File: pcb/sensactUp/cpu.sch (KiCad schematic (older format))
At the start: 25 parts, among them P16 CONN_01X04, P17 CONN_01X04, P3 CONN_01X02, SW1 SW_PUSH, SW2 SW_PUSH, SW3 SW_PUSH, X1 8MHz

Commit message: Huge Refactoring; still untested
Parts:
- removed C10, C11, C4, C7, C8, C9: 100n, Capacitors_SMD:C_0805_HandSoldering, symbol C-RESCUE-multiupbox
- removed C5, C6: 27p, Capacitors_SMD:C_0805_HandSoldering, symbol C-RESCUE-multiupbox
- removed D19: LED, Resistors_SMD:R_0805_HandSoldering, symbol LED-RESCUE-multiupbox
- removed L1: INDUCTOR, Inductors_NEOSID:Neosid_Inductor_SM1206, symbol INDUCTOR
- removed P16, P17: CONN_01X04, Pin_Headers:Pin_Header_Straight_1x04, symbol CONN_01X04
- removed P3: CONN_01X02, Pin_Headers:Pin_Header_Straight_1x02, symbol CONN_01X02
- removed R24, R25, R3, R31, R32: 10k, Resistors_SMD:R_0805_HandSoldering, symbol R-RESCUE-multiupbox
- removed R30: 330R, Resistors_SMD:R_0805_HandSoldering, symbol R-RESCUE-multiupbox
- removed R5: 1M, Resistors_SMD:R_0805_HandSoldering, symbol R-RESCUE-multiupbox
- removed SW1, SW2, SW3: SW_PUSH, Discret:SW_PUSH_SMALL, symbol SW_PUSH
- removed U?: STM32F103CB, LQFP48, symbol STM32F103CB
- removed X1: 8MHz, Crystals:Crystal_HC49-U_Vertical, symbol CRYSTAL
- added C15: 4u7, Capacitors_SMD:C_1206_HandSoldering, symbol C
- added C16, C17, C18: u1, Capacitors_SMD:C_0805_HandSoldering, symbol C
- added C19: 10n, Capacitors_SMD:C_0805_HandSoldering, symbol C
- added C20: 1u, Capacitors_SMD:C_0805_HandSoldering, symbol C
- added C7, C8: 22p, Capacitors_SMD:C_0805_HandSoldering, symbol C
- added FB1: FILTER, Resistors_SMD:R_1206_HandSoldering, symbol FILTER
- added P7: CONN_01X06, sensact:MicroUsbVertical, symbol CONN_01X06
- added R10: M1, Resistors_SMD:R_0805_HandSoldering, symbol R
- added R7: 220R, Resistors_SMD:R_0805_HandSoldering, symbol R
- added U3: STM32F072C8Tx, sensact:LQFP-48_7x7mm_Pitch0.5mm_handsolder, symbol STM32F072C8Tx
- added Y1: Crystal_GND24, sensact:quartz3225, symbol Crystal_GND24
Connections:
- net labels added: +3.3VA, CANR, CANT, INT1, INT2, INT3, IO1, IO2, IO3, IO4, IO5, IO6, IO7, IO8, ROTA, ROTB, ROTD, RX, SCL, SCL1, SDA, SDA1, SHDN, SWCLK, SWDIO, TX, USBM, USBP, WS2812, xROTA, xROTB, xROTD
- net labels removed: BOOT0, PA0, PA1, PA10, PA11, PA12, PA13, PA14, PA15, PA2, PA3, PA4, PA5, PA6, PA7, PA8, PA9, PA[0..15], PB0, PB1, PB10, PB11, PB12, PB13, PB14, PB15, PB2, PB3, PB4, PB5, PB6, PB7, PB8, PB9, PB[0..15], PC0, PC1, PC10, PC11, PC12, PC13, PC14, PC15, PC2, PC3, PC4, PC5, PC6, PC7, PC8, PC9, PC[0..15], PD2
- wire segments 118 -> 67
- no-connect marks 1 -> 5
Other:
- note removed: "DCF77-Modul (Pollin)"
- note removed: "Programmer-Anschluss"
- note removed: "i2c-Anschluss"

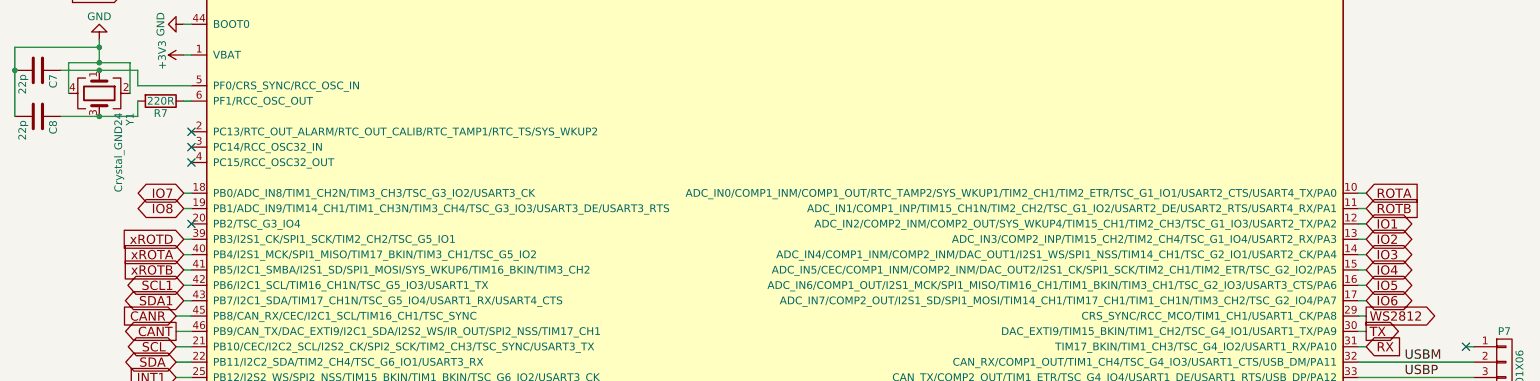
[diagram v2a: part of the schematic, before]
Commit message: SensactUP gets LIN-Port and alternative 5V Power Supply
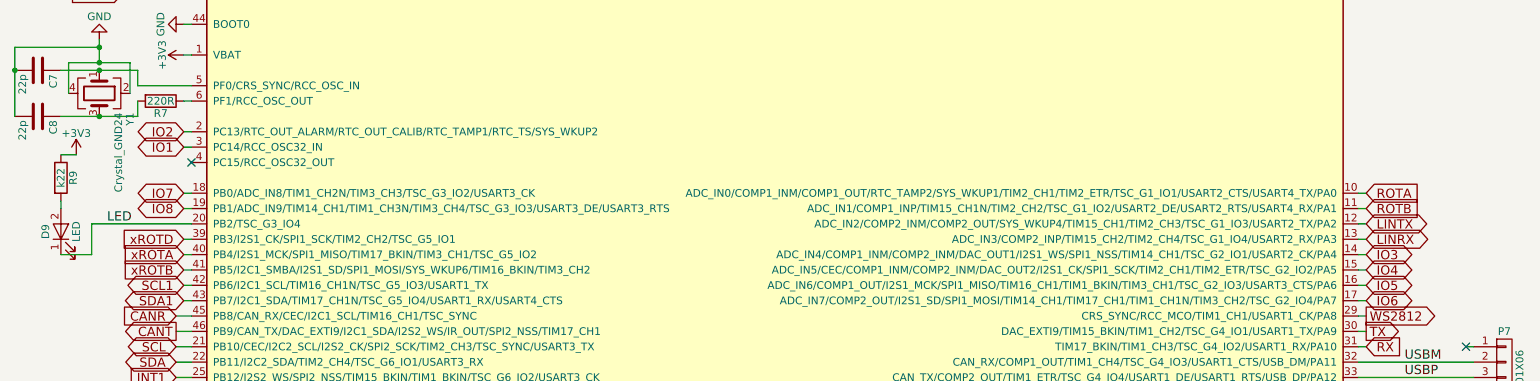
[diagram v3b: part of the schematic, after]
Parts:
- added D9: LED, sensact:LED_0805_handsolder, symbol LED
- added R9: k22, Resistors_SMD:R_0805_HandSoldering, symbol R
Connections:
- net +3V3: now also R9.1
- net IO1: now also U3.3 (PC14/RCC_OSC32_IN); no longer U3.12 (ADC_IN2/COMP2_INM/COMP2_OUT/SYS_WKUP4/TIM15_CH1/TIM2_CH3/TSC_G1_IO3/USART2_TX/PA2)
- net IO2: now also U3.2 (PC13/RTC_OUT_ALARM/RTC_OUT_CALIB/RTC_TAMP1/RTC_TS/SYS_WKUP2); no longer U3.13 (ADC_IN3/COMP2_INP/TIM15_CH2/TIM2_CH4/TSC_G1_IO4/USART2_RX/PA3)
- net LED: now reaches U3.20 (PB2/TSC_G3_IO4)
- net LED: now also D9.1 (K)
- new net: D9.2 (A), R9.2
- new net LINRX: U3.13 (ADC_IN3/COMP2_INP/TIM15_CH2/TIM2_CH4/TSC_G1_IO4/USART2_RX/PA3)
- new net LINTX: U3.12 (ADC_IN2/COMP2_INM/COMP2_OUT/SYS_WKUP4/TIM15_CH1/TIM2_CH3/TSC_G1_IO3/USART2_TX/PA2)
- no-connect marks 5 -> 2
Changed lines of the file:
@@
 LIBS:relays
 LIBS:sensact
+LIBS:mechanical
 LIBS:sensactUp-cache
 EELAYER 25 0
@@
 $EndComp
 $Comp
-L +3V3 #PWR031
+L +3V3 #PWR035
 U 1 1 58B75879
 P 5350 1650
-F 0 "#PWR031" H 5350 1500 50  0001 C CNN
+F 0 "#PWR035" H 5350 1500 50  0001 C CNN
 F 1 "+3V3" H 5350 1790 50  0000 C CNN
 F 2 "" H 5350 1650 50  0000 C CNN
@@
 $EndComp
 $Comp
-L +3V3 #PWR032
+L +3V3 #PWR036
 U 1 1 58B7589B
 P 5600 1650
-F 0 "#PWR032" H 5600 1500 50  0001 C CNN
+F 0 "#PWR036" H 5600 1500 50  0001 C CNN
 F 1 "+3V3" H 5600 1790 50  0000 C CNN
 F 2 "" H 5600 1650 50  0000 C CNN
@@
 Connection ~ 5350 1650
 $Comp
-L +3.3VA #PWR033
+L +3.3VA #PWR037
 U 1 1 58B75979
 P 5500 1450
-F 0 "#PWR033" H 5500 1300 50  0001 C CNN
+F 0 "#PWR037" H 5500 1300 50  0001 C CNN
 F 1 "+3.3VA" H 5500 1590 50  0000 C CNN
 F 2 "" H 5500 1450 50  0000 C CNN
@@
 Connection ~ 4700 1150
 $Comp
-L +3.3VA #PWR034
+L +3.3VA #PWR038
 U 1 1 58B759CE
 P 4800 950
-F 0 "#PWR034" H 4800 800 50  0001 C CNN
+F 0 "#PWR038" H 4800 800 50  0001 C CNN
 F 1 "+3.3VA" H 4800 1090 50  0000 C CNN
 F 2 "" H 4800 950 50  0000 C CNN
@@
 Connection ~ 3450 1150
 $Comp
-L +3V3 #PWR035
+L +3V3 #PWR039
 U 1 1 58B75AF2
 P 3550 1100
-F 0 "#PWR035" H 3550 950 50  0001 C CNN
+F 0 "#PWR039" H 3550 950 50  0001 C CNN
 F 1 "+3V3" H 3550 1240 50  0000 C CNN
 F 2 "" H 3550 1100 50  0000 C CNN
@@
 Connection ~ 3450 1450
 $Comp
-L GND #PWR036
+L GND #PWR040
 U 1 1 58B75BBF
 P 3550 1500
-F 0 "#PWR036" H 3550 1250 50  0001 C CNN
+F 0 "#PWR040" H 3550 1250 50  0001 C CNN
 F 1 "GND" H 3550 1350 50  0000 C CNN
 F 2 "" H 3550 1500 50  0000 C CNN
@@
 Connection ~ 3550 1450
 $Comp
-L GND #PWR037
+L GND #PWR041
 U 1 1 58B75C63
 P 5450 5450
-F 0 "#PWR037" H 5450 5200 50  0001 C CNN
+F 0 "#PWR041" H 5450 5200 50  0001 C CNN
 F 1 "GND" H 5450 5300 50  0000 C CNN
 F 2 "" H 5450 5450 50  0000 C CNN
@@
 	1700 2200 1250 2200
 $Comp
-L GND #PWR038
+L GND #PWR042
 U 1 1 58B775D8
 P 1650 2400
-F 0 "#PWR038" H 1650 2150 50  0001 C CNN
+F 0 "#PWR042" H 1650 2150 50  0001 C CNN
 F 1 "GND" H 1650 2250 50  0000 C CNN
 F 2 "" H 1650 2400 50  0000 C CNN
@@
 $EndComp
 $Comp
-L +3V3 #PWR039
+L +3V3 #PWR043
 U 1 1 58B775FC
 P 1650 2600
-F 0 "#PWR039" H 1650 2450 50  0001 C CNN
+F 0 "#PWR043" H 1650 2450 50  0001 C CNN
 F 1 "+3V3" H 1650 2740 50  0000 C CNN
 F 2 "" H 1650 2600 50  0000 C CNN
@@
 	900  2650 900  2850
 $Comp
-L GND #PWR040
+L GND #PWR044
 U 1 1 58B7775E
 P 1100 2500
-F 0 "#PWR040" H 1100 2250 50  0001 C CNN
+F 0 "#PWR044" H 1100 2250 50  0001 C CNN
 F 1 "GND" H 1100 2350 50  0000 C CNN
 F 2 "" H 1100 2500 50  0000 C CNN
@@
 ROTB
 Text GLabel 9350 3700 2    60   BiDi ~ 0
-IO1
+LINTX
 Text GLabel 9350 3800 2    60   BiDi ~ 0
-IO2
+LINRX
 Text GLabel 9350 3900 2    60   BiDi ~ 0
 IO3
@@
 	9850 4800 10050 4800
 $Comp
-L GND #PWR041
+L GND #PWR045
 U 1 1 58B845F6
 P 10050 5150
-F 0 "#PWR041" H 10050 4900 50  0001 C CNN
+F 0 "#PWR045" H 10050 4900 50  0001 C CNN
 F 1 "GND" H 10050 5000 50  0000 C CNN
 F 2 "" H 10050 5150 50  0000 C CNN
@@
 Wire Wire Line
 	1700 4000 1650 4000
-NoConn ~ 1700 3100
-NoConn ~ 1700 3200
 NoConn ~ 1700 3300
-NoConn ~ 1700 3700
 Text Label 9600 4600 0    60   ~ 0
 USBM
@@
 	1700 4200 1650 4200
 $Comp
-L PWR_FLAG #FLG042
+L PWR_FLAG #FLG046
 U 1 1 58BB5186
 P 4900 1100
-F 0 "#FLG042" H 4900 1195 50  0001 C CNN
+F 0 "#FLG046" H 4900 1195 50  0001 C CNN
 F 1 "PWR_FLAG" H 4900 1280 50  0000 C CNN
 F 2 "" H 4900 1100 50  0000 C CNN
@@
 	4900 1150 4900 1100
 Connection ~ 4900 1150
+Text GLabel 1650 3200 0    60   BiDi ~ 0
+IO1
+Text GLabel 1650 3100 0    60   BiDi ~ 0
+IO2
+Wire Wire Line
+	1700 3100 1650 3100
+Wire Wire Line
+	1700 3200 1650 3200
+$Comp
+L R R9
+U 1 1 595FEA9F
+P 850 3400
+F 0 "R9" V 930 3400 50  0000 C CNN
+F 1 "k22" V 850 3400 50  0000 C CNN
+F 2 "Resistors_SMD:R_0805_HandSoldering" V 780 3400 50  0001 C CNN
+F 3 "" H 850 3400 50  0000 C CNN
+	1    850  3400
+	1    0    0    -1
+$EndComp
+$Comp
+L LED D9
+U 1 1 595FEC87
+P 850 3750
+F 0 "D9" H 850 3850 50  0000 C CNN
+F 1 "LED" H 850 3650 50  0000 C CNN
+F 2 "sensact:LED_0805_handsolder" H 850 3750 50  0001 C CNN
+F 3 "" H 850 3750 50  0000 C CNN
+	1    850  3750
+	0    -1   -1   0
+$EndComp
+Wire Wire Line
+	1700 3700 1050 3700
+Wire Wire Line
+	1050 3700 1050 3900
+Wire Wire Line
+	1050 3900 850  3900
+Wire Wire Line
+	850  3550 850  3600
+$Comp
+L +3V3 #PWR047
+U 1 1 595FEDC0
+P 950 3250
+F 0 "#PWR047" H 950 3100 50  0001 C CNN
+F 1 "+3V3" H 950 3390 50  0000 C CNN
+F 2 "" H 950 3250 50  0000 C CNN
+F 3 "" H 950 3250 50  0000 C CNN
+	1    950  3250
+	1    0    0    -1
+$EndComp
+Wire Wire Line
+	950  3250 850  3250
+Text Label 1150 3700 0    60   ~ 0
+LED
 $EndSCHEMATC

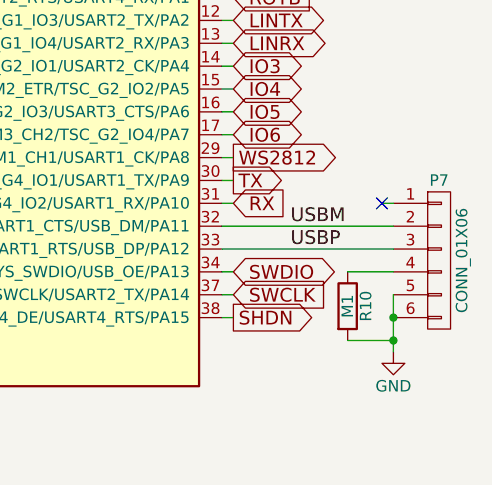
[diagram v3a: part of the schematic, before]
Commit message: sensactUP - going further
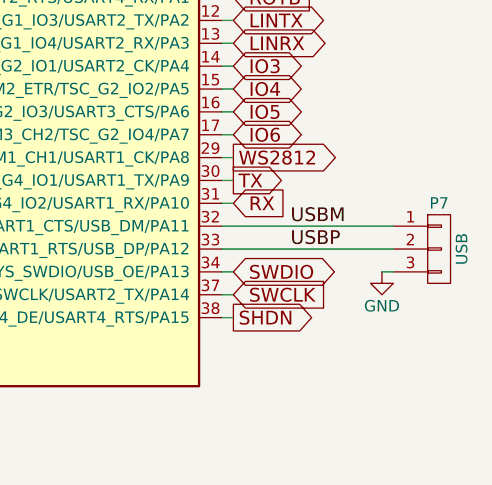
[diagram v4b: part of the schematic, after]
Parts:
- removed P7: CONN_01X06, sensact:MicroUsbVertical, symbol CONN_01X06
- removed R10: M1, Resistors_SMD:R_0805_HandSoldering, symbol R
- added P7: USB, Pin_Headers:Pin_Header_Straight_1x03_Pitch2.00mm, symbol CONN_01X03
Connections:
- net GND: now also P7.3 (P3)
- net USBM: now also P7.1 (P1)
- net USBP: now also P7.2 (P2)
- no-connect marks 2 -> 1
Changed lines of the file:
@@
 $EndComp
 $Comp
-L +3V3 #PWR035
+L +3V3 #PWR058
 U 1 1 58B75879
 P 5350 1650
-F 0 "#PWR035" H 5350 1500 50  0001 C CNN
+F 0 "#PWR058" H 5350 1500 50  0001 C CNN
 F 1 "+3V3" H 5350 1790 50  0000 C CNN
 F 2 "" H 5350 1650 50  0000 C CNN
@@
 $EndComp
 $Comp
-L +3V3 #PWR036
+L +3V3 #PWR059
 U 1 1 58B7589B
 P 5600 1650
-F 0 "#PWR036" H 5600 1500 50  0001 C CNN
+F 0 "#PWR059" H 5600 1500 50  0001 C CNN
 F 1 "+3V3" H 5600 1790 50  0000 C CNN
 F 2 "" H 5600 1650 50  0000 C CNN
@@
 Connection ~ 5350 1650
 $Comp
-L +3.3VA #PWR037
+L +3.3VA #PWR060
 U 1 1 58B75979
 P 5500 1450
-F 0 "#PWR037" H 5500 1300 50  0001 C CNN
+F 0 "#PWR060" H 5500 1300 50  0001 C CNN
 F 1 "+3.3VA" H 5500 1590 50  0000 C CNN
 F 2 "" H 5500 1450 50  0000 C CNN
@@
 Connection ~ 4700 1150
 $Comp
-L +3.3VA #PWR038
+L +3.3VA #PWR061
 U 1 1 58B759CE
 P 4800 950
-F 0 "#PWR038" H 4800 800 50  0001 C CNN
+F 0 "#PWR061" H 4800 800 50  0001 C CNN
 F 1 "+3.3VA" H 4800 1090 50  0000 C CNN
 F 2 "" H 4800 950 50  0000 C CNN
@@
 Connection ~ 3450 1150
 $Comp
-L +3V3 #PWR039
+L +3V3 #PWR062
 U 1 1 58B75AF2
 P 3550 1100
-F 0 "#PWR039" H 3550 950 50  0001 C CNN
+F 0 "#PWR062" H 3550 950 50  0001 C CNN
 F 1 "+3V3" H 3550 1240 50  0000 C CNN
 F 2 "" H 3550 1100 50  0000 C CNN
@@
 Connection ~ 3450 1450
 $Comp
-L GND #PWR040
+L GND #PWR063
 U 1 1 58B75BBF
 P 3550 1500
-F 0 "#PWR040" H 3550 1250 50  0001 C CNN
+F 0 "#PWR063" H 3550 1250 50  0001 C CNN
 F 1 "GND" H 3550 1350 50  0000 C CNN
 F 2 "" H 3550 1500 50  0000 C CNN
@@
 Connection ~ 3550 1450
 $Comp
-L GND #PWR041
+L GND #PWR064
 U 1 1 58B75C63
 P 5450 5450
-F 0 "#PWR041" H 5450 5200 50  0001 C CNN
+F 0 "#PWR064" H 5450 5200 50  0001 C CNN
 F 1 "GND" H 5450 5300 50  0000 C CNN
 F 2 "" H 5450 5450 50  0000 C CNN
@@
 	1700 2200 1250 2200
 $Comp
-L GND #PWR042
+L GND #PWR065
 U 1 1 58B775D8
 P 1650 2400
-F 0 "#PWR042" H 1650 2150 50  0001 C CNN
+F 0 "#PWR065" H 1650 2150 50  0001 C CNN
 F 1 "GND" H 1650 2250 50  0000 C CNN
 F 2 "" H 1650 2400 50  0000 C CNN
@@
 $EndComp
 $Comp
-L +3V3 #PWR043
+L +3V3 #PWR066
 U 1 1 58B775FC
 P 1650 2600
-F 0 "#PWR043" H 1650 2450 50  0001 C CNN
+F 0 "#PWR066" H 1650 2450 50  0001 C CNN
 F 1 "+3V3" H 1650 2740 50  0000 C CNN
 F 2 "" H 1650 2600 50  0000 C CNN
@@
 	900  2650 900  2850
 $Comp
-L GND #PWR044
+L GND #PWR067
 U 1 1 58B7775E
 P 1100 2500
-F 0 "#PWR044" H 1100 2250 50  0001 C CNN
+F 0 "#PWR067" H 1100 2250 50  0001 C CNN
 F 1 "GND" H 1100 2350 50  0000 C CNN
 F 2 "" H 1100 2500 50  0000 C CNN
@@
 Wire Wire Line
 	1700 4400 1600 4400
-NoConn ~ 10000 4500
-$Comp
-L R R10
-U 1 1 58B84475
-P 9850 4950
-F 0 "R10" V 9930 4950 50  0000 C CNN
-F 1 "M1" V 9850 4950 50  0000 C CNN
-F 2 "Resistors_SMD:R_0805_HandSoldering" V 9780 4950 50  0001 C CNN
-F 3 "" H 9850 4950 50  0000 C CNN
-	1    9850 4950
-	1    0    0    -1
-$EndComp
-Wire Wire Line
-	9850 4800 10050 4800
-$Comp
-L GND #PWR045
+$Comp
+L GND #PWR068
 U 1 1 58B845F6
-P 10050 5150
-F 0 "#PWR045" H 10050 4900 50  0001 C CNN
-F 1 "GND" H 10050 5000 50  0000 C CNN
-F 2 "" H 10050 5150 50  0000 C CNN
-F 3 "" H 10050 5150 50  0000 C CNN
-	1    10050 5150
-	1    0    0    -1
-$EndComp
-$Comp
-L CONN_01X06 P7
-U 1 1 58B84694
-P 10250 4750
-F 0 "P7" H 10250 5100 50  0000 C CNN
-F 1 "CONN_01X06" V 10350 4750 50  0000 C CNN
-F 2 "sensact:MicroUsbVertical" H 10250 4750 50  0001 C CNN
-F 3 "" H 10250 4750 50  0000 C CNN
-	1    10250 4750
-	1    0    0    -1
-$EndComp
-Wire Wire Line
-	10050 4500 10000 4500
-Wire Wire Line
-	10050 4900 10050 5150
-Wire Wire Line
-	10050 5100 9850 5100
-Connection ~ 10050 5000
-Connection ~ 10050 5100
+P 10000 4800
+F 0 "#PWR068" H 10000 4550 50  0001 C CNN
+F 1 "GND" H 10000 4650 50  0000 C CNN
+F 2 "" H 10000 4800 50  0000 C CNN
+F 3 "" H 10000 4800 50  0000 C CNN
+	1    10000 4800
+	1    0    0    -1
+$EndComp
 Text GLabel 9350 5000 2    60   Output ~ 0
 SHDN
@@
 Wire Wire Line
 	1700 4000 1650 4000
-NoConn ~ 1700 3300
 Text Label 9600 4600 0    60   ~ 0
 USBM
@@
 	1700 4200 1650 4200
 $Comp
-L PWR_FLAG #FLG046
+L PWR_FLAG #FLG069
 U 1 1 58BB5186
 P 4900 1100
-F 0 "#FLG046" H 4900 1195 50  0001 C CNN
+F 0 "#FLG069" H 4900 1195 50  0001 C CNN
 F 1 "PWR_FLAG" H 4900 1280 50  0000 C CNN
 F 2 "" H 4900 1100 50  0000 C CNN
@@
 	850  3550 850  3600
 $Comp
-L +3V3 #PWR047
+L +3V3 #PWR070
 U 1 1 595FEDC0
 P 950 3250
-F 0 "#PWR047" H 950 3100 50  0001 C CNN
+F 0 "#PWR070" H 950 3100 50  0001 C CNN
 F 1 "+3V3" H 950 3390 50  0000 C CNN
 F 2 "" H 950 3250 50  0000 C CNN
@@
 Text Label 1150 3700 0    60   ~ 0
 LED
+$Comp
+L CONN_01X03 P7
+U 1 1 59694EB9
+P 10250 4700
+F 0 "P7" H 10250 4900 50  0000 C CNN
+F 1 "USB" V 10350 4700 50  0000 C CNN
+F 2 "Pin_Headers:Pin_Header_Straight_1x03_Pitch2.00mm" H 10250 4700 50  0001 C CNN
+F 3 "" H 10250 4700 50  0000 C CNN
+	1    10250 4700
+	1    0    0    -1
+$EndComp
+Wire Wire Line
+	10050 4800 10000 4800
+NoConn ~ 1700 3300
 $EndSCHEMATC

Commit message: Unspecified
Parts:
- Y1: value Crystal_GND24 -> 16MHz
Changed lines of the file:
@@
 P 1100 2850
 F 0 "Y1" H 1225 3050 50  0000 L CNN
-F 1 "Crystal_GND24" H 1225 2975 50  0000 L CNN
+F 1 "16MHz" H 1225 2975 50  0000 L CNN
 F 2 "sensact:quartz3225" H 1100 2850 50  0001 C CNN
 F 3 "" H 1100 2850 50  0000 C CNN

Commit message: WHS lIb
WHS lIb
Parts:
- C15, C16, C17, C18, C19, C20, C7, C8: symbol C -> Device:C
- D9: symbol LED -> Device:LED
- FB1: symbol FILTER -> sensactUp-rescue:FILTER
- P7: symbol CONN_01X03 -> sensactUp-rescue:CONN_01X03
- R7, R9: symbol R -> Device:R
- U3: symbol STM32F072C8Tx -> sensactUp-rescue:STM32F072C8Tx
- Y1: symbol Crystal_GND24 -> Device:Crystal_GND24
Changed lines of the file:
@@
-EESchema Schematic File Version 2
-LIBS:power
-LIBS:device
-LIBS:transistors
-LIBS:conn
-LIBS:linear
-LIBS:regul
-LIBS:74xx
-LIBS:cmos4000
-LIBS:adc-dac
-LIBS:memory
-LIBS:xilinx
-LIBS:microcontrollers
-LIBS:dsp
-LIBS:microchip
-LIBS:analog_switches
-LIBS:motorola
-LIBS:texas
-LIBS:intel
-LIBS:audio
-LIBS:interface
-LIBS:digital-audio
-LIBS:philips
-LIBS:display
-LIBS:cypress
-LIBS:siliconi
-LIBS:opto
-LIBS:atmel
-LIBS:contrib
-LIBS:valves
-LIBS:stm32
-LIBS:switches
-LIBS:relays
-LIBS:sensact
-LIBS:mechanical
+EESchema Schematic File Version 4
 LIBS:sensactUp-cache
-EELAYER 25 0
+EELAYER 26 0
 EELAYER END
 $Descr A4 11693 8268
@@
 $EndDescr
 $Comp
-L STM32F072C8Tx U3
+L sensactUp-rescue:STM32F072C8Tx U3
 U 1 1 58B753F2
 P 5500 3600
@@
 $EndComp
 $Comp
-L C C19
+L Device:C C19
 U 1 1 58B754C8
 P 4700 1300
@@
 $EndComp
 $Comp
-L C C20
+L Device:C C20
 U 1 1 58B754E7
 P 4900 1300
@@
 $EndComp
 $Comp
-L C C15
+L Device:C C15
 U 1 1 58B75545
 P 3250 1300
@@
 $EndComp
 $Comp
-L C C18
+L Device:C C18
 U 1 1 58B7557A
 P 3850 1300
@@
 $EndComp
 $Comp
-L C C17
+L Device:C C17
 U 1 1 58B755AD
 P 3650 1300
@@
 $EndComp
 $Comp
-L C C16
+L Device:C C16
 U 1 1 58B755D0
 P 3450 1300
@@
 $EndComp
 $Comp
-L +3V3 #PWR057
+L power:+3V3 #PWR057
 U 1 1 58B75879
 P 5350 1650
@@
 $EndComp
 $Comp
-L +3V3 #PWR058
+L power:+3V3 #PWR058
 U 1 1 58B7589B
 P 5600 1650
@@
 	5400 1650 5400 1700
 Wire Wire Line
-	5300 1650 5400 1650
+	5300 1650 5350 1650
 Wire Wire Line
 	5300 1700 5300 1650
 Connection ~ 5350 1650
 $Comp
-L +3.3VA #PWR059
+L power:+3.3VA #PWR059
 U 1 1 58B75979
 P 5500 1450
@@
 Connection ~ 4700 1150
 $Comp
-L +3.3VA #PWR060
+L power:+3.3VA #PWR060
 U 1 1 58B759CE
 P 4800 950
@@
 Connection ~ 4800 1150
 Wire Wire Line
-	3250 1150 3950 1150
+	3250 1150 3450 1150
 Connection ~ 3850 1150
 Connection ~ 3650 1150
 Connection ~ 3450 1150
 $Comp
-L +3V3 #PWR061
+L power:+3V3 #PWR061
 U 1 1 58B75AF2
 P 3550 1100
@@
 Connection ~ 3550 1150
 Wire Wire Line
-	3250 1450 4900 1450
+	3250 1450 3450 1450
 Connection ~ 4700 1450
 Connection ~ 3850 1450
@@
 Connection ~ 3450 1450
 $Comp
-L GND #PWR062
+L power:GND #PWR062
 U 1 1 58B75BBF
 P 3550 1500
@@
 Connection ~ 3550 1450
 $Comp
-L GND #PWR063
+L power:GND #PWR063
 U 1 1 58B75C63
 P 5450 5450
@@
 $EndComp
 Wire Wire Line
-	5300 5450 5600 5450
+	5300 5450 5400 5450
 Wire Wire Line
 	5600 5450 5600 5400
@@
 Connection ~ 5400 5450
 $Comp
-L FILTER FB1
+L sensactUp-rescue:FILTER FB1
 U 1 1 58B76153
 P 4300 1150
@@
 $EndComp
 Wire Wire Line
-	4650 1150 4900 1150
+	4650 1150 4700 1150
 Text GLabel 1250 2200 0    60   Input ~ 0
 NRST
@@
 	1700 2200 1250 2200
 $Comp
-L GND #PWR064
+L power:GND #PWR064
 U 1 1 58B775D8
 P 1650 2400
@@
 $EndComp
 $Comp
-L +3V3 #PWR065
+L power:+3V3 #PWR065
 U 1 1 58B775FC
 P 1650 2600
@@
 	1700 2600 1650 2600
 $Comp
-L Crystal_GND24 Y1
+L Device:Crystal_GND24 Y1
 U 1 1 58B7767E
 P 1100 2850
@@
 	1350 2700 1350 2800
 Wire Wire Line
-	850  2700 1350 2700
-Wire Wire Line
-	850  3000 1350 3000
+	850  2700 1100 2700
+Wire Wire Line
+	850  3000 1100 3000
 Wire Wire Line
 	1350 3000 1350 2900
@@
 	1300 2650 1300 2850
 Wire Wire Line
-	900  2650 1300 2650
+	900  2650 1100 2650
 Wire Wire Line
 	900  2650 900  2850
 $Comp
-L GND #PWR066
+L power:GND #PWR066
 U 1 1 58B7775E
 P 1100 2500
@@
 $EndComp
 Wire Wire Line
-	1100 2500 1100 2650
+	1100 2500 1100 2550
 Connection ~ 1100 2650
 $Comp
-L R R7
+L Device:R R7
 U 1 1 58B777BB
 P 1500 2900
@@
 	1350 2800 1700 2800
 $Comp
-L C C7
+L Device:C C7
 U 1 1 58B779D4
 P 700 2700
@@
 $EndComp
 $Comp
-L C C8
+L Device:C C8
 U 1 1 58B77A09
 P 700 3000
@@
 Connection ~ 1100 3000
 Wire Wire Line
-	550  2550 550  3000
+	550  2550 550  2700
 Wire Wire Line
 	550  2550 1100 2550
@@
 	1700 4400 1600 4400
 $Comp
-L GND #PWR067
+L power:GND #PWR067
 U 1 1 58B845F6
 P 10000 4800
@@
 	1700 4200 1650 4200
 $Comp
-L PWR_FLAG #FLG068
+L power:PWR_FLAG #FLG068
 U 1 1 58BB5186
 P 4900 1100
@@
 	1700 3200 1650 3200
 $Comp
-L R R9
+L Device:R R9
 U 1 1 595FEA9F
 P 850 3400
@@
 $EndComp
 $Comp
-L LED D9
+L Device:LED D9
 U 1 1 595FEC87
 P 850 3750
@@
 	850  3550 850  3600
 $Comp
-L +3V3 #PWR069
+L power:+3V3 #PWR069
 U 1 1 595FEDC0
 P 950 3250
@@
 LED
 $Comp
-L CONN_01X03 P7
+L sensactUp-rescue:CONN_01X03 P7
 U 1 1 59694EB9
 P 10250 4700
@@
 	10050 4800 10000 4800
 NoConn ~ 1700 3300
+Wire Wire Line
+	5350 1650 5400 1650
+Wire Wire Line
+	4700 1150 4800 1150
+Wire Wire Line
+	4800 1150 4900 1150
+Wire Wire Line
+	3850 1150 3950 1150
+Wire Wire Line
+	3650 1150 3850 1150
+Wire Wire Line
+	3450 1150 3550 1150
+Wire Wire Line
+	3550 1150 3650 1150
+Wire Wire Line
+	4700 1450 4900 1450
+Wire Wire Line
+	3850 1450 4700 1450
+Wire Wire Line
+	3650 1450 3850 1450
+Wire Wire Line
+	3450 1450 3550 1450
+Wire Wire Line
+	3550 1450 3650 1450
+Wire Wire Line
+	5500 5450 5600 5450
+Wire Wire Line
+	5450 5450 5500 5450
+Wire Wire Line
+	5400 5450 5450 5450
+Wire Wire Line
+	1100 2650 1300 2650
+Wire Wire Line
+	1100 2700 1350 2700
+Wire Wire Line
+	1100 3000 1350 3000
+Wire Wire Line
+	1100 2550 1100 2650
+Wire Wire Line
+	550  2700 550  3000
 $EndSCHEMATC
